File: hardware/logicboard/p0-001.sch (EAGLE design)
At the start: 23 parts, among them IC1 74LS07N, IC2 LTC485N, IC3 LTC485N

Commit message: New layout.
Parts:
- renumbered MIDIRX to RX, MIDITX to TX, PWR to PWR5V
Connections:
- net MIDIRX- renamed MIDIIN-
- removed net MIDIRX+: MIDIIN.1, R3.2
- removed net MIDITX+: MIDIOUT.1, R1.1
- removed net MIDITX-: MIDIOUT.3, R2.2
- new net MIDIIN+: MIDIIN.1, R1.2
- new net MIDIOUT+: MIDIOUT.1, R2.1
- new net MIDIOUT-: MIDIOUT.3, R3.2
- net N$15: now also R1.1; no longer R3.1
- net N$2: now also R3.1; no longer R2.1
- net RX+: now also R7.2; no longer R6.2
- net RX-: now also R7.1; no longer R6.1
- net TX+: now also R6.2; no longer R7.2
- net TX-: now also R6.1; no longer R7.1
- net VCC: now also R2.2; no longer R1.2
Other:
- note added: "Pineapple Zero 1.0.0 Copyright 2015-2018 by Pineapple Design"
- note removed: "MIDI Longranger 1.0.0 Copyright 2015-2018 by Pineapple Design"
- moved on the sheet: D1, IC1A, IC1B, IC1C, IC1D, IC1E, R1, R2, R3, R4, R5, R6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

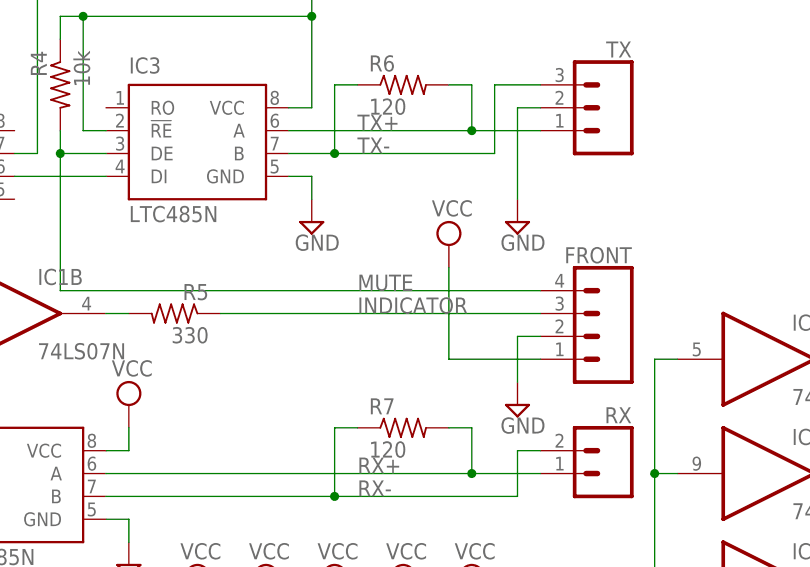
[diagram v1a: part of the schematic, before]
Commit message: Changed signal names.
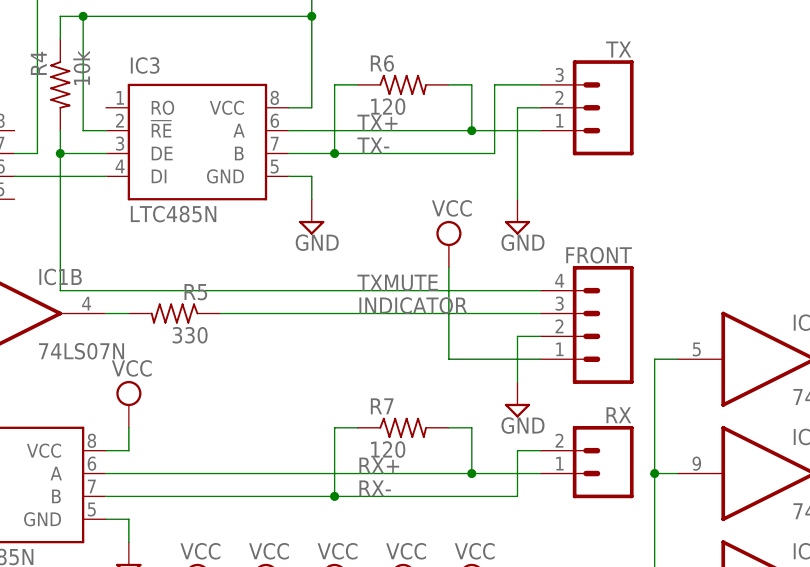
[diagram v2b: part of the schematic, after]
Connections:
- net COM1 renamed RX
- net MUTE renamed TXMUTE
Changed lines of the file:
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@@
 <setting verticaltext="up"/>
 </settings>
-<grid distance="0.1" unitdist="inch" unit="inch" style="dots" multiple="1" display="yes" altdistance="0.01" altunitdist="inch" altunit="inch"/>
+<grid distance="0.1" unitdist="inch" unit="inch" style="lines" multiple="1" display="no" altdistance="0.01" altunitdist="inch" altunit="inch"/>
 <layers>
 <layer number="1" name="Top" color="4" fill="1" visible="no" active="no"/>
@@
 </segment>
 </net>
-<net name="COM1" class="0">
+<net name="RX" class="0">
 <segment>
 <pinref part="IC2" gate="G$1" pin="RO"/>
@@
 </segment>
 </net>
-<net name="MUTE" class="0">
+<net name="TXMUTE" class="0">
 <segment>
 <pinref part="R4" gate="G$1" pin="2"/>

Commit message: OSHW logo.
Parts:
- added LOGO1: OSHW-LOGOS, SparkFun-Aesthetics:OSHW-LOGOS
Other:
- note added: "Pineapple Zero 1.0.1"
- note removed: "Pineapple Zero 1.0.0 Copyright 2015-2018 by Pineapple Design"
- moved on the sheet: C1, C2, C3, C4, C5, D1, FRONT, IC1A, IC1B, IC1C, IC1D, IC1E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

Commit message: Pineapple logo v2.
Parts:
- added U$1: PINEAPPLELOGO2, pineapplelogo2:PINEAPPLELOGO2
- LOGO1: value OSHW-LOGOS -> OSHW-LOGOS-COPPER; device SparkFun-Aesthetics:OSHW-LOGOS -> SparkFun-Aesthetics:OSHW-LOGOS-COPPER
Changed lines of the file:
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@@
 <part name="SUPPLY23" library="supply2" library_urn="urn:adsk.eagle:library:372" deviceset="GND" device=""/>
 <part name="FRAME1" library="frames" library_urn="urn:adsk.eagle:library:229" deviceset="A4L-LOC" device=""/>
-<part name="LOGO1" library="SparkFun-Aesthetics" deviceset="OSHW-LOGO" device="S"/>
+<part name="U$1" library="pineapplelogo2" deviceset="PINEAPPLELOGO2" device=""/>
+<part name="LOGO1" library="SparkFun-Aesthetics" deviceset="OSHW-LOGO" device="S-COPPER"/>
 </parts>
 <sheets>
@@
 <instance part="SUPPLY23" gate="GND" x="144.78" y="71.12"/>
 <instance part="FRAME1" gate="G$1" x="0" y="0"/>
-<instance part="LOGO1" gate="G$1" x="200.66" y="15.24"/>
+<instance part="U$1" gate="G$1" x="187.96" y="7.62"/>
+<instance part="LOGO1" gate="G$1" x="241.3" y="165.1"/>
 </instances>
 <busses>

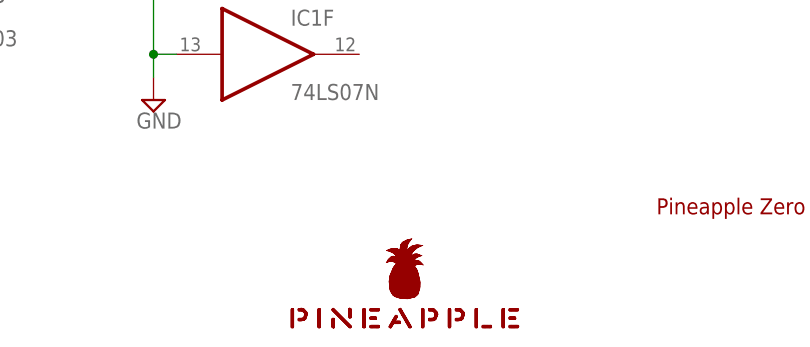
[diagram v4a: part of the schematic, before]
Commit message: New pineapple logo.
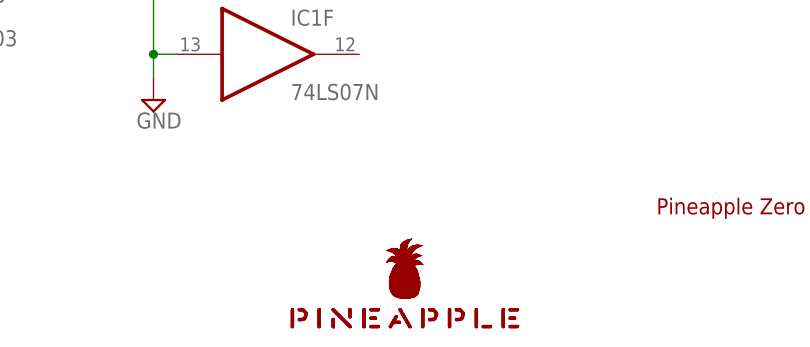
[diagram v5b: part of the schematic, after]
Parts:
- LOGO1: value OSHW-LOGOS-COPPER -> OSHW-LOGOS; device SparkFun-Aesthetics:OSHW-LOGOS-COPPER -> SparkFun-Aesthetics:OSHW-LOGOS
- U$1: value PINEAPPLELOGO2 -> PINEAPPLELOGO2SILKMINI; device pineapplelogo2:PINEAPPLELOGO2 -> pineapplelogo:PINEAPPLELOGO2SILKMINI
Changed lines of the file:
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@@
 <part name="SUPPLY23" library="supply2" library_urn="urn:adsk.eagle:library:372" deviceset="GND" device=""/>
 <part name="FRAME1" library="frames" library_urn="urn:adsk.eagle:library:229" deviceset="A4L-LOC" device=""/>
-<part name="U$1" library="pineapplelogo2" deviceset="PINEAPPLELOGO2" device=""/>
-<part name="LOGO1" library="SparkFun-Aesthetics" deviceset="OSHW-LOGO" device="S-COPPER"/>
+<part name="LOGO1" library="SparkFun-Aesthetics" deviceset="OSHW-LOGO" device="S" value="OSHW-LOGOS"/>
+<part name="U$1" library="pineapplelogo" deviceset="PINEAPPLELOGO2SILKMINI" device=""/>
 </parts>
 <sheets>
@@
 <instance part="SUPPLY23" gate="GND" x="144.78" y="71.12"/>
 <instance part="FRAME1" gate="G$1" x="0" y="0"/>
+<instance part="LOGO1" gate="G$1" x="241.3" y="165.1"/>
 <instance part="U$1" gate="G$1" x="187.96" y="7.62"/>
-<instance part="LOGO1" gate="G$1" x="241.3" y="165.1"/>
 </instances>
 <busses>

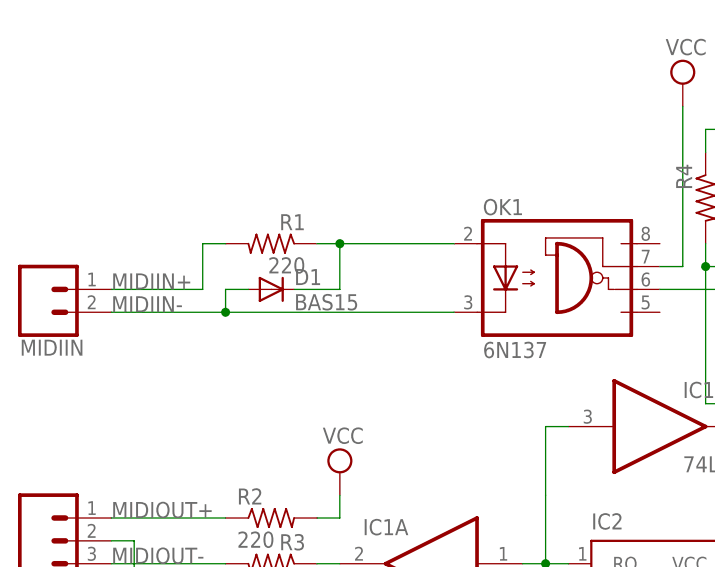
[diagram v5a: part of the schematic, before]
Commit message: Replaced D1.
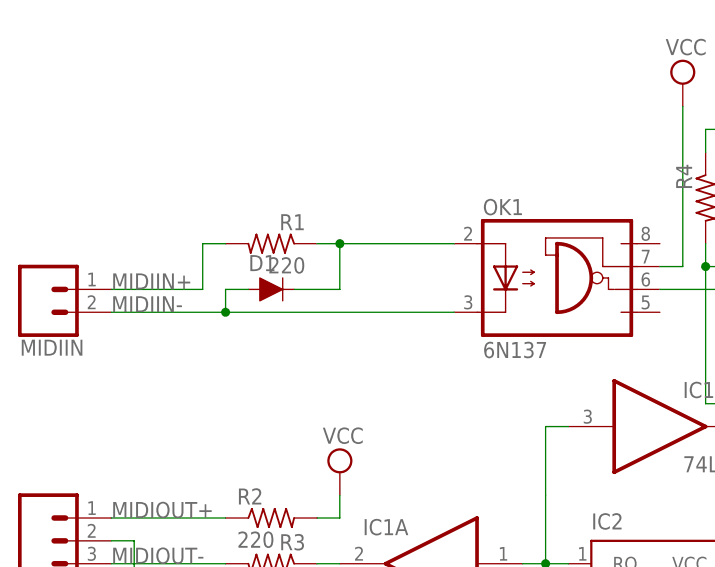
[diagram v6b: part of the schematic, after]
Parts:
- D1: value BAS15 -> DIODE-1N4148; device diode:BAS15 -> SparkFun-DiscreteSemi:DIODE-1N4148
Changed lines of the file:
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@@
 <part name="R1" library="resistor" library_urn="urn:adsk.eagle:library:348" deviceset="R-US_" device="0204/5" package3d_urn="urn:adsk.eagle:package:25955/1" value="220"/>
 <part name="OK1" library="optocoupler" library_urn="urn:adsk.eagle:library:320" deviceset="6N137" device="" package3d_urn="urn:adsk.eagle:package:21941/1"/>
-<part name="D1" library="diode" library_urn="urn:adsk.eagle:library:210" deviceset="BAS15" device="" package3d_urn="urn:adsk.eagle:package:43348/1"/>
+<part name="D1" library="SparkFun-DiscreteSemi" library_urn="urn:adsk.eagle:library:514" deviceset="DIODE" device="-1N4148" package3d_urn="urn:adsk.eagle:package:38452/1" value=""/>
 <part name="IC2" library="linear-technology" library_urn="urn:adsk.eagle:library:261" deviceset="LTC485" device="N" package3d_urn="urn:adsk.eagle:package:16059/1"/>
 <part name="IC3" library="linear-technology" library_urn="urn:adsk.eagle:library:261" deviceset="LTC485" device="N" package3d_urn="urn:adsk.eagle:package:16059/1"/>
@@
 <instance part="R1" gate="G$1" x="45.72" y="101.6" rot="MR0"/>
 <instance part="OK1" gate="A" x="78.74" y="96.52"/>
-<instance part="D1" gate="1" x="45.72" y="96.52"/>
+<instance part="D1" gate="G$1" x="45.72" y="96.52"/>
 <instance part="IC2" gate="G$1" x="88.9" y="63.5"/>
 <instance part="IC3" gate="G$1" x="109.22" y="101.6"/>
@@
 <net name="N$15" class="0">
 <segment>
-<pinref part="D1" gate="1" pin="C"/>
+<pinref part="D1" gate="G$1" pin="C"/>
 <wire x1="48.26" y1="96.52" x2="53.34" y2="96.52" width="0.1524" layer="91"/>
 <wire x1="53.34" y1="96.52" x2="53.34" y2="101.6" width="0.1524" layer="91"/>
@@
 <net name="MIDIIN-" class="0">
 <segment>
-<pinref part="D1" gate="1" pin="A"/>
+<pinref part="D1" gate="G$1" pin="A"/>
 <wire x1="40.64" y1="93.98" x2="40.64" y2="96.52" width="0.1524" layer="91"/>
 <wire x1="40.64" y1="96.52" x2="43.18" y2="96.52" width="0.1524" layer="91"/>

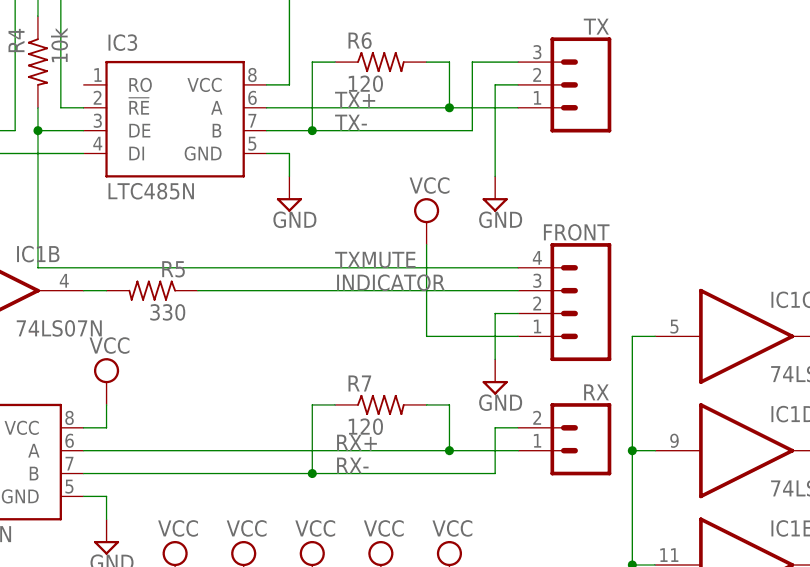
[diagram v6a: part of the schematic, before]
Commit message: Changed signal names.
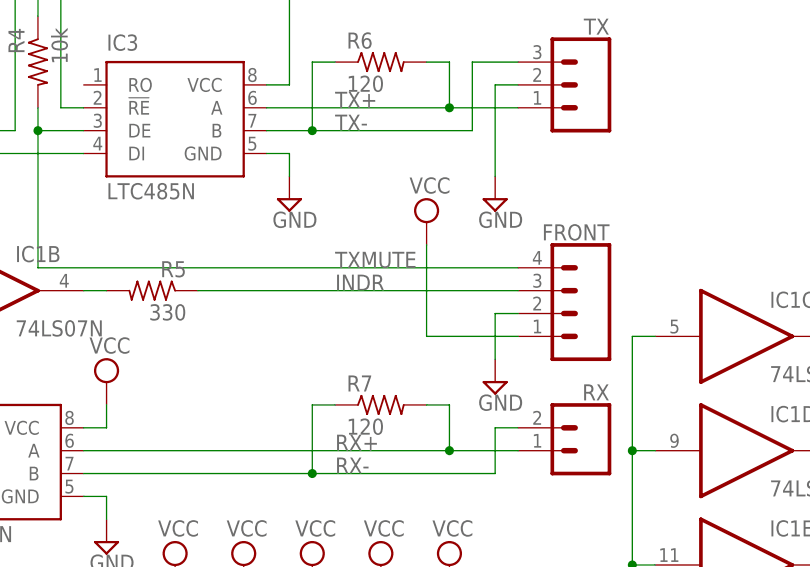
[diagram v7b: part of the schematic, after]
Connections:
- net COM2 renamed MIDIIN
- net INDICATOR renamed INDR
- net N$15 renamed MIDIINA
- net N$2 renamed MIDIOUT-RAW
- net N$3 renamed IND
- net RX renamed MIDIOUT
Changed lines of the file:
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@@
 </segment>
 </net>
-<net name="N$2" class="0">
+<net name="MIDIOUT-RAW" class="0">
 <segment>
 <pinref part="R3" gate="G$1" pin="1"/>
@@
 </segment>
 </net>
-<net name="N$15" class="0">
+<net name="MIDIINA" class="0">
 <segment>
 <pinref part="D1" gate="G$1" pin="C"/>
@@
 </segment>
 </net>
-<net name="COM2" class="0">
+<net name="MIDIIN" class="0">
 <segment>
 <pinref part="OK1" gate="A" pin="VO"/>
@@
 </segment>
 </net>
-<net name="RX" class="0">
+<net name="MIDIOUT" class="0">
 <segment>
 <pinref part="IC2" gate="G$1" pin="RO"/>
@@
 </segment>
 </net>
-<net name="N$3" class="0">
+<net name="IND" class="0">
 <segment>
 <pinref part="IC1" gate="B" pin="O"/>
@@
 </segment>
 </net>
-<net name="INDICATOR" class="0">
+<net name="INDR" class="0">
 <segment>
 <pinref part="FRONT" gate="G$1" pin="3"/>

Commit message: Version 1.0.1 -> 1.1.0.
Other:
- note added: "Pineapple Zero 1.1.0"
- note removed: "Pineapple Zero 1.0.1"
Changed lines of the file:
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@@
 <sheet>
 <plain>
-<text x="215.9" y="20.32" size="1.778" layer="94">Pineapple Zero 1.0.1</text>
+<text x="215.9" y="20.32" size="1.778" layer="94">Pineapple Zero 1.1.0</text>
 </plain>
 <instances>
